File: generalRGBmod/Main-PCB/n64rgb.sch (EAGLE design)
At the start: 71 parts, among them J1 MY_JUMPER, U1 5M570ZT100C5, U2 THS7374, U3 TLV70018-DDC

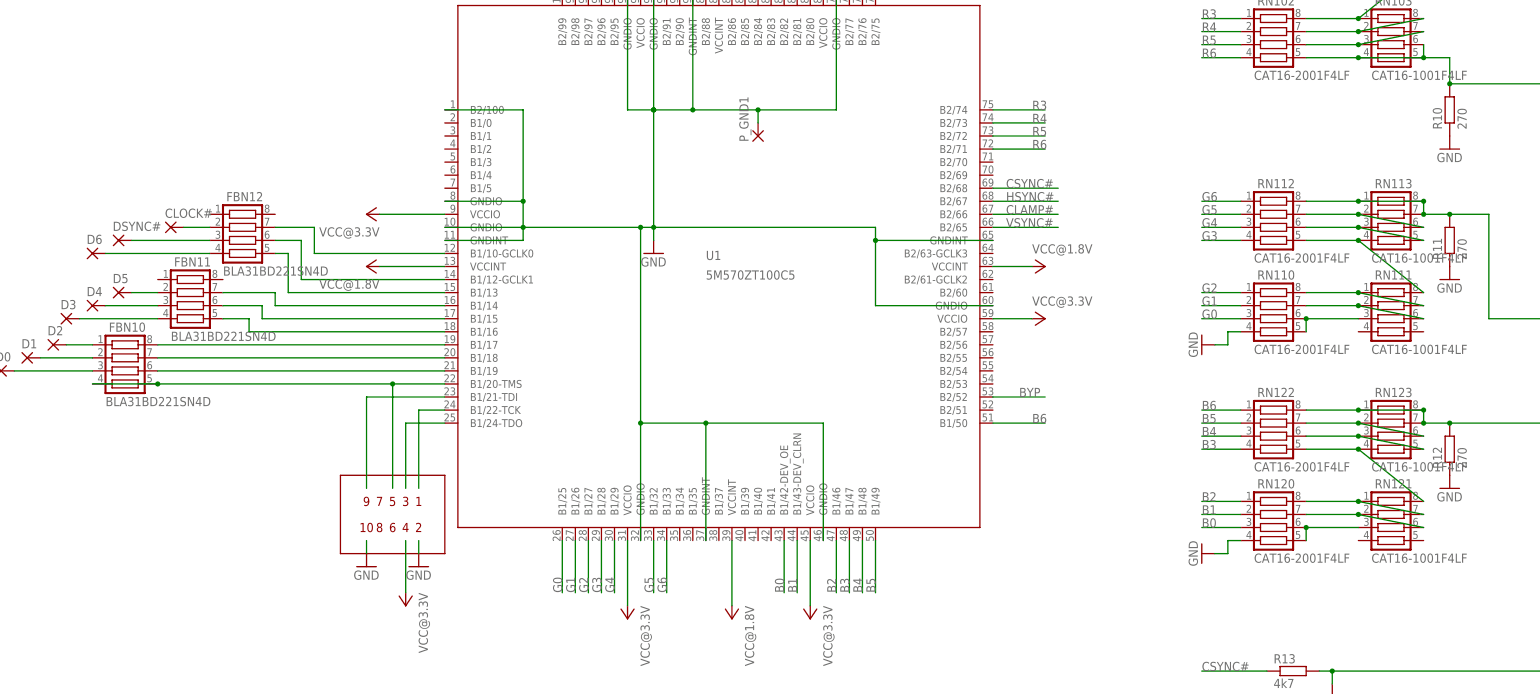
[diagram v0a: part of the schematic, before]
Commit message: PCB Update: - rotate JTAG header by 180deg - pull-ups and -downs for TCK, TMS and TDI as recommended by Altera / Intel - thicker wire for Vcc near pad
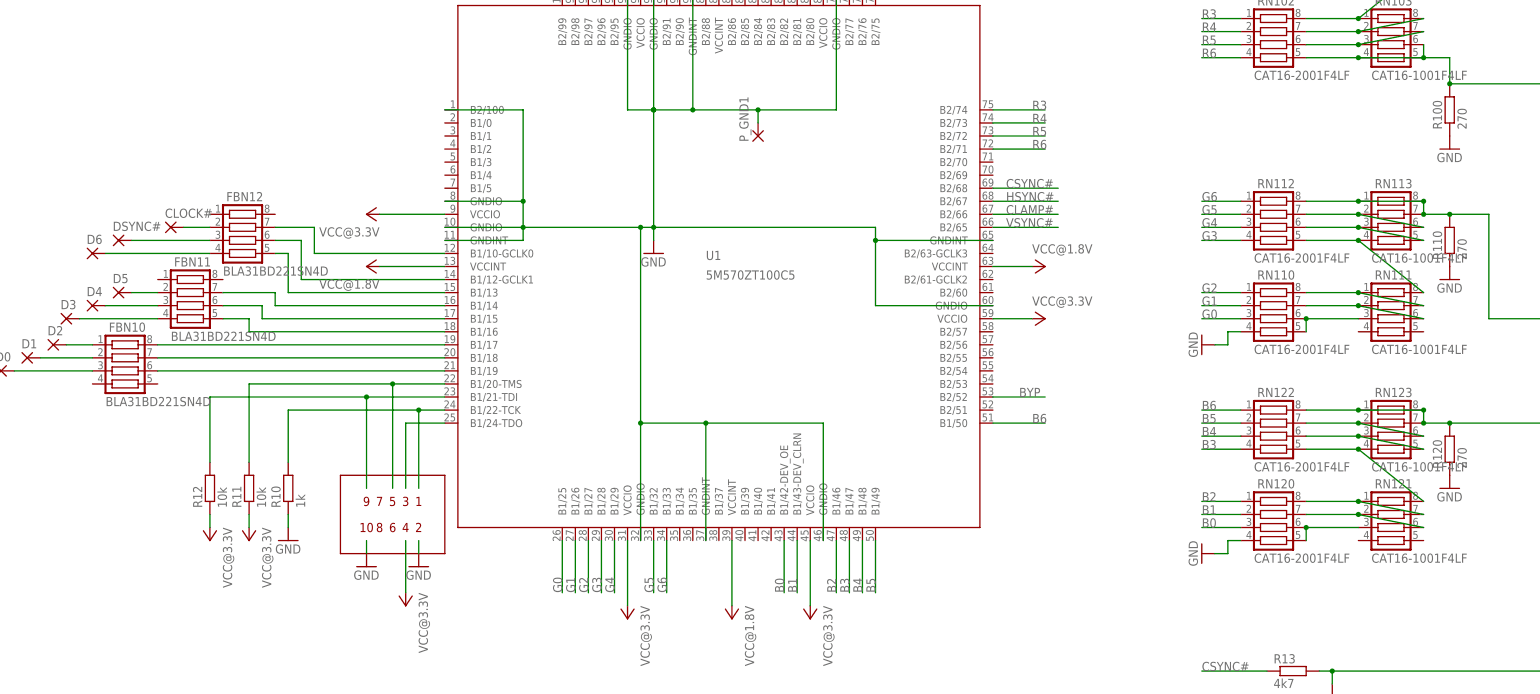
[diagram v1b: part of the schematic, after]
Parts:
- added R100, R110, R120: 270, rcl:R-EU_R0603
- R10: value 270 -> 1k
- R11, R12: value 270 -> 10k
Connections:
- net GND: now also R100.1, R110.1, R120.1; no longer R11.1, R12.1
- net N$31: now also R120.2; no longer R12.2
- net N$48: now also R100.2; no longer R10.2
- net N$76: now also R110.2; no longer R11.2
- net TCK: now also R10.2
- net TDI: now also R12.2
- net TMS: now also R11.2; no longer FBN10.4, FBN10.5
- net VCC@3.3V: now also R11.1, R12.1
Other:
- moved on the sheet: R10, R11, R12
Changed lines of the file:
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@@
 <?xml version="1.0" encoding="utf-8"?>
 <!DOCTYPE eagle SYSTEM "eagle.dtd">
-<eagle version="7.7.0">
+<eagle version="8.2.1">
 <drawing>
 <settings>
@@
 <part name="RN101" library="resistor-net" deviceset="CTS742C083" device="" value="CAT16-1001F4LF "/>
 <part name="RN103" library="resistor-net" deviceset="CTS742C083" device="" value="CAT16-1001F4LF "/>
-<part name="R10" library="rcl" deviceset="R-EU_" device="R0603" value="270"/>
+<part name="R100" library="rcl" deviceset="R-EU_" device="R0603" value="270"/>
 <part name="GND22" library="supply1" deviceset="GND" device=""/>
 <part name="RN20" library="resistor-net" deviceset="CTS742C083" device="" value="CAT16-75R0F4LF "/>
@@
 <part name="RN111" library="resistor-net" deviceset="CTS742C083" device="" value="CAT16-1001F4LF "/>
 <part name="RN113" library="resistor-net" deviceset="CTS742C083" device="" value="CAT16-1001F4LF "/>
-<part name="R11" library="rcl" deviceset="R-EU_" device="R0603" value="270"/>
+<part name="R110" library="rcl" deviceset="R-EU_" device="R0603" value="270"/>
 <part name="GND9" library="supply1" deviceset="GND" device=""/>
 <part name="RN120" library="resistor-net" deviceset="CTS742C083" device="" value="CAT16-2001F4LF "/>
@@
 <part name="RN121" library="resistor-net" deviceset="CTS742C083" device="" value="CAT16-1001F4LF "/>
 <part name="RN123" library="resistor-net" deviceset="CTS742C083" device="" value="CAT16-1001F4LF "/>
-<part name="R12" library="rcl" deviceset="R-EU_" device="R0603" value="270"/>
+<part name="R120" library="rcl" deviceset="R-EU_" device="R0603" value="270"/>
 <part name="GND10" library="supply1" deviceset="GND" device=""/>
 <part name="DSYNC#" library="wirepad" deviceset="SMD1" device="" value=""/>
@@
 <part name="FBN13" library="resistor-net" deviceset="CTS742C083" device="" value="BLA31BD221SN4D "/>
 <part name="J1" library="snes_div" deviceset="MY_JUMPER" device="" value=""/>
+<part name="R10" library="rcl" deviceset="R-EU_" device="R0603" value="1k"/>
+<part name="R11" library="rcl" deviceset="R-EU_" device="R0603" value="10k"/>
+<part name="R12" library="rcl" deviceset="R-EU_" device="R0603" value="10k"/>
+<part name="P+2" library="supply1" deviceset="VCC" device="" value="VCC@3.3V"/>
+<part name="P+18" library="supply1" deviceset="VCC" device="" value="VCC@3.3V"/>
+<part name="GND3" library="supply1" deviceset="GND" device=""/>
 </parts>
 <sheets>
@@
 <instance part="RN101" gate="G$1" x="274.32" y="185.42"/>
 <instance part="RN103" gate="G$1" x="274.32" y="167.64"/>
-<instance part="R10" gate="G$1" x="287.02" y="152.4" rot="R90"/>
+<instance part="R100" gate="G$1" x="287.02" y="152.4" rot="R90"/>
 <instance part="GND22" gate="1" x="287.02" y="144.78"/>
 <instance part="RN20" gate="G$1" x="373.38" y="104.14"/>
@@
 <instance part="RN111" gate="G$1" x="274.32" y="114.3"/>
 <instance part="RN113" gate="G$1" x="274.32" y="132.08"/>
-<instance part="R11" gate="G$1" x="287.02" y="127" rot="R90"/>
+<instance part="R110" gate="G$1" x="287.02" y="127" rot="R90"/>
 <instance part="GND9" gate="1" x="287.02" y="119.38"/>
 <instance part="RN120" gate="G$1" x="251.46" y="73.66"/>
@@
 <instance part="RN121" gate="G$1" x="274.32" y="73.66"/>
 <instance part="RN123" gate="G$1" x="274.32" y="91.44"/>
-<instance part="R12" gate="G$1" x="287.02" y="86.36" rot="R90"/>
+<instance part="R120" gate="G$1" x="287.02" y="86.36" rot="R90"/>
 <instance part="GND10" gate="1" x="287.02" y="78.74"/>
 <instance part="DSYNC#" gate="G$1" x="27.94" y="127"/>
@@
 <instance part="FBN13" gate="G$1" x="91.44" y="187.96"/>
 <instance part="J1" gate="G$1" x="101.6" y="248.92"/>
+<instance part="R10" gate="G$1" x="60.96" y="78.74" rot="R90"/>
+<instance part="R11" gate="G$1" x="53.34" y="78.74" rot="R90"/>
+<instance part="R12" gate="G$1" x="45.72" y="78.74" rot="R90"/>
+<instance part="P+2" gate="VCC" x="53.34" y="68.58" rot="R180"/>
+<instance part="P+18" gate="VCC" x="45.72" y="68.58" rot="R180"/>
+<instance part="GND3" gate="1" x="60.96" y="68.58"/>
 </instances>
 <busses>
@@
 </segment>
 <segment>
-<pinref part="R10" gate="G$1" pin="1"/>
+<pinref part="R100" gate="G$1" pin="1"/>
 <pinref part="GND22" gate="1" pin="GND"/>
 </segment>
@@
 </segment>
 <segment>
-<pinref part="R11" gate="G$1" pin="1"/>
+<pinref part="R110" gate="G$1" pin="1"/>
 <pinref part="GND9" gate="1" pin="GND"/>
 </segment>
 <segment>
-<pinref part="R12" gate="G$1" pin="1"/>
+<pinref part="R120" gate="G$1" pin="1"/>
 <pinref part="GND10" gate="1" pin="GND"/>
 </segment>
@@
 <pinref part="GND11" gate="1" pin="GND"/>
 <wire x1="86.36" y1="66.04" x2="86.36" y2="68.58" width="0.1524" layer="91"/>
+</segment>
+<segment>
+<pinref part="R10" gate="G$1" pin="1"/>
+<pinref part="GND3" gate="1" pin="GND"/>
+<wire x1="60.96" y1="71.12" x2="60.96" y2="73.66" width="0.1524" layer="91"/>
 </segment>
 </net>
@@
 <wire x1="83.82" y1="58.42" x2="83.82" y2="68.58" width="0.1524" layer="91"/>
 </segment>
+<segment>
+<pinref part="R11" gate="G$1" pin="1"/>
+<pinref part="P+2" gate="VCC" pin="VCC"/>
+<wire x1="53.34" y1="71.12" x2="53.34" y2="73.66" width="0.1524" layer="91"/>
+</segment>
+<segment>
+<pinref part="R12" gate="G$1" pin="1"/>
+<pinref part="P+18" gate="VCC" pin="VCC"/>
+<wire x1="45.72" y1="71.12" x2="45.72" y2="73.66" width="0.1524" layer="91"/>
+</segment>
 </net>
 <net name="N$2" class="0">
@@
 <wire x1="91.44" y1="93.98" x2="86.36" y2="93.98" width="0.1524" layer="91"/>
 <wire x1="86.36" y1="93.98" x2="86.36" y2="78.74" width="0.1524" layer="91"/>
+<pinref part="R10" gate="G$1" pin="2"/>
+<wire x1="86.36" y1="93.98" x2="60.96" y2="93.98" width="0.1524" layer="91"/>
+<wire x1="60.96" y1="93.98" x2="60.96" y2="83.82" width="0.1524" layer="91"/>
+<junction x="86.36" y="93.98"/>
 </segment>
 </net>
@@
 <wire x1="91.44" y1="96.52" x2="76.2" y2="96.52" width="0.1524" layer="91"/>
 <wire x1="76.2" y1="96.52" x2="76.2" y2="78.74" width="0.1524" layer="91"/>
+<pinref part="R12" gate="G$1" pin="2"/>
+<wire x1="76.2" y1="96.52" x2="45.72" y2="96.52" width="0.1524" layer="91"/>
+<wire x1="45.72" y1="96.52" x2="45.72" y2="83.82" width="0.1524" layer="91"/>
+<junction x="76.2" y="96.52"/>
 </segment>
 </net>
@@
 <pinref part="U1" gate="G$1" pin="B1/20-TMS"/>
 <wire x1="81.28" y1="99.06" x2="81.28" y2="78.74" width="0.1524" layer="91"/>
-<pinref part="FBN10" gate="G$1" pin="5"/>
-<wire x1="81.28" y1="99.06" x2="35.56" y2="99.06" width="0.1524" layer="91"/>
+<pinref part="R11" gate="G$1" pin="2"/>
+<wire x1="81.28" y1="99.06" x2="53.34" y2="99.06" width="0.1524" layer="91"/>
+<wire x1="53.34" y1="99.06" x2="53.34" y2="83.82" width="0.1524" layer="91"/>
 <junction x="81.28" y="99.06"/>
-<pinref part="FBN10" gate="G$1" pin="4"/>
-<wire x1="35.56" y1="99.06" x2="22.86" y2="99.06" width="0.1524" layer="91"/>
-<junction x="35.56" y="99.06"/>
 </segment>
 </net>
@@
 <wire x1="287.02" y1="132.08" x2="294.64" y2="132.08" width="0.1524" layer="91"/>
 <wire x1="294.64" y1="132.08" x2="294.64" y2="111.76" width="0.1524" layer="91"/>
-<pinref part="R11" gate="G$1" pin="2"/>
+<pinref part="R110" gate="G$1" pin="2"/>
 <junction x="287.02" y="132.08"/>
 <pinref part="RN112" gate="G$1" pin="8"/>
@@
 <pinref part="RN123" gate="G$1" pin="7"/>
 <wire x1="281.94" y1="91.44" x2="287.02" y2="91.44" width="0.1524" layer="91"/>
-<pinref part="R12" gate="G$1" pin="2"/>
+<pinref part="R120" gate="G$1" pin="2"/>
 <junction x="287.02" y="91.44"/>
 <pinref part="RN122" gate="G$1" pin="8"/>
@@
 <pinref part="RN102" gate="G$1" pin="5"/>
 <wire x1="259.08" y1="162.56" x2="269.24" y2="162.56" width="0.1524" layer="91"/>
-<pinref part="R10" gate="G$1" pin="2"/>
+<pinref part="R100" gate="G$1" pin="2"/>
 <wire x1="287.02" y1="157.48" x2="327.66" y2="157.48" width="0.1524" layer="91"/>
 <wire x1="327.66" y1="157.48" x2="327.66" y2="104.14" width="0.1524" layer="91"/>
